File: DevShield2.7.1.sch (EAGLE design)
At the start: 58 parts, among them Q1 BC846BWT1G, SW1 BC-RESET, SW2 ARD-RESET, SW3 RECLAIM, U1 LD1117S33TR, U2 74LVC241A, U3 ETRX357, U4 SN74LVC1G32, U5 ER-OLED9.1, U6 AT45DB041D, X1 ISA HEADER, X3 RASPBERRYPI-V2-HEADERS, X4 1X5

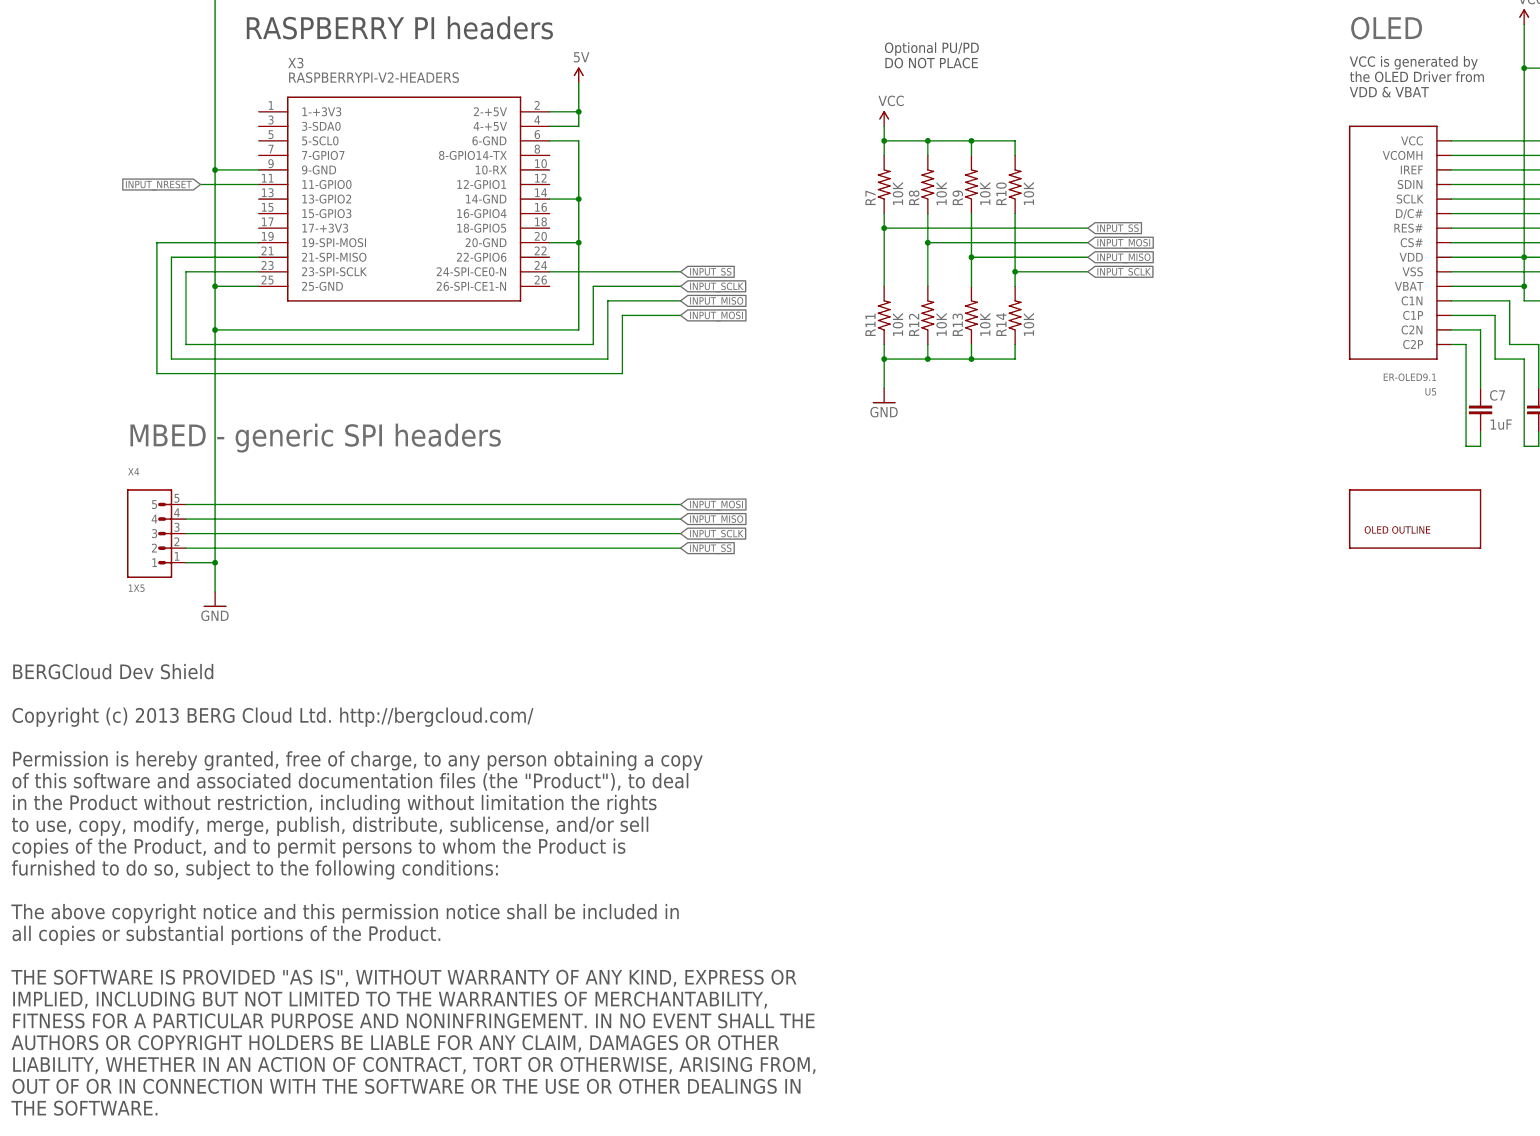
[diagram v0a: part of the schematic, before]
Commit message: Updated Library and pin names for Raspberry Pi
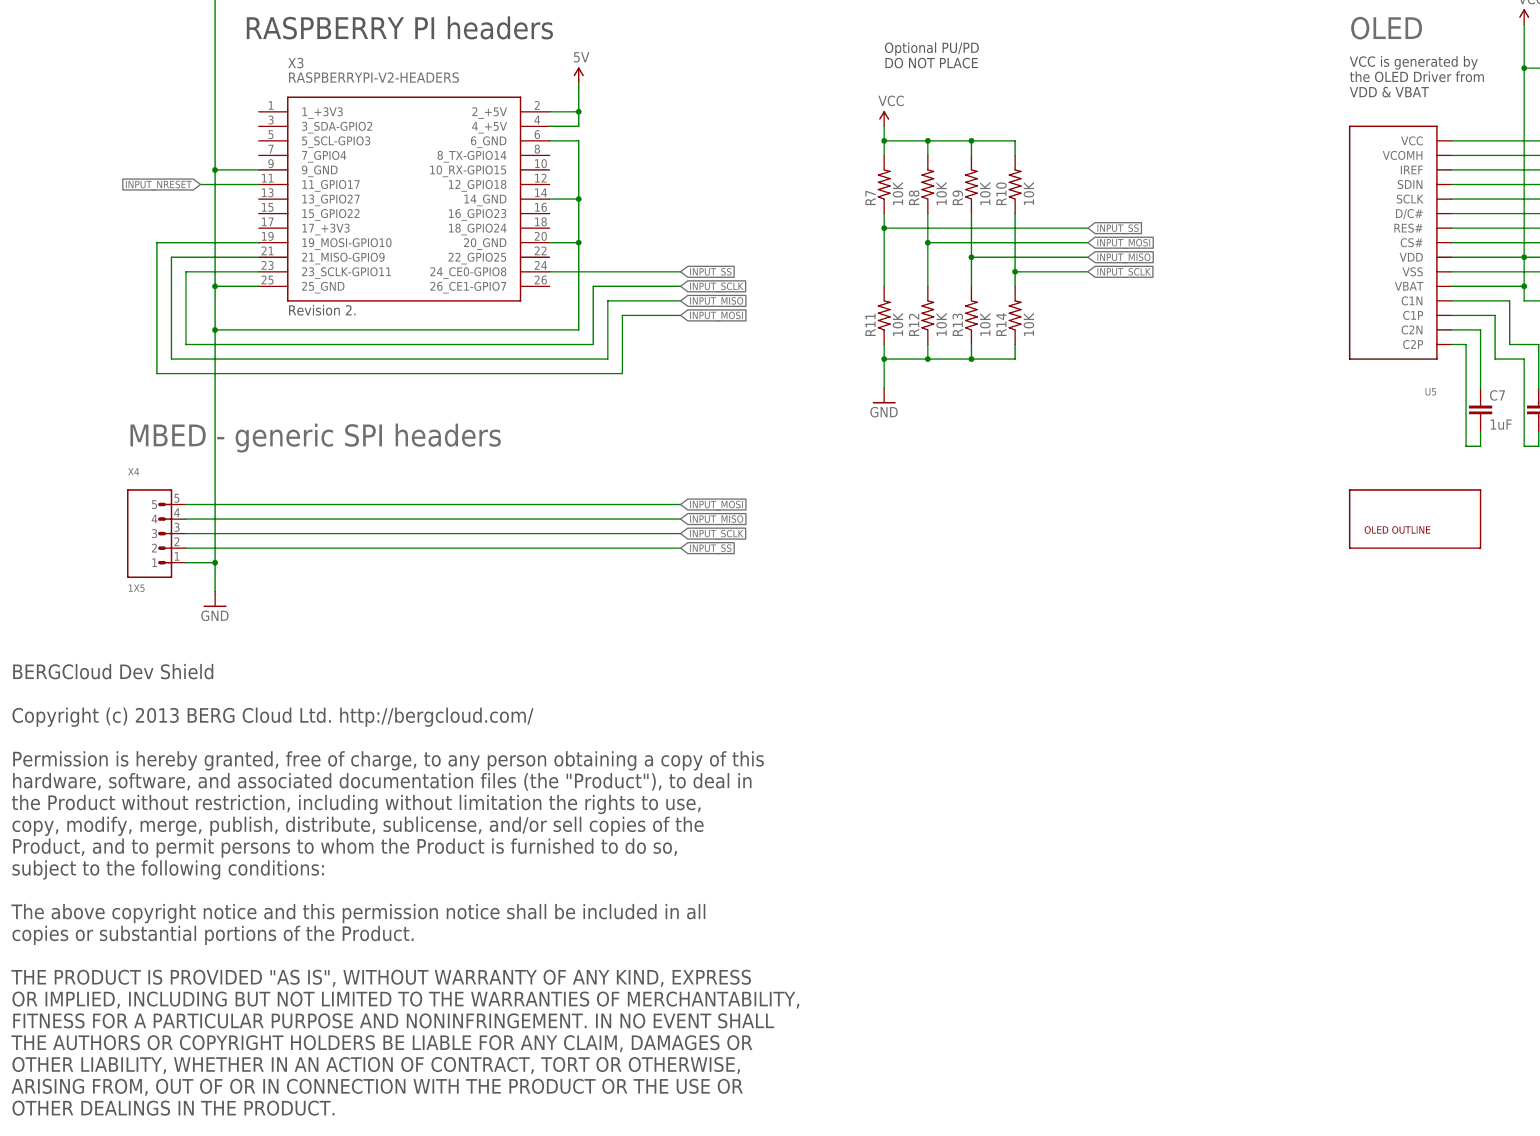
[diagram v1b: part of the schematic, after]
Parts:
- IGNORE: value OLED -> ER-OLED0.91-1-OUTLINE; device BERG-Eagle_Library:OLED -> BERGCloud-OSH:ER-OLED0.91-1-OUTLINE
- Q1: device BERG-Eagle_Library:BC846BWT1GTRANSISTOR -> BERGCloud-OSH:BC846BWT1G
- SW1, SW2: device BERG-Eagle_Library:SPST -> BERGCloud-OSH:SPST
- U1: device BERG-OSH:LD1117S33TR -> BERGCloud-OSH:LD1117S33TR
- U2: device BERG-OSH:74LVC241APW -> BERGCloud-OSH:74LVC241APW
- U3: device BERG-OSH:ETRX35XMODULE-SMD -> BERGCloud-OSH:ETRX35XMODULE-SMD
- U4: device BERG-OSH:74LVC1G32 -> BERGCloud-OSH:74LVC1G32
- U5: value ER-OLED9.1 -> ER-OLED0.91-1HANDSOLDER_BOTTOMLAYER; device BERG-Eagle_Library:ER-OLED9.1 -> BERGCloud-OSH:ER-OLED0.91-1HANDSOLDER_BOTTOMLAYER
- X1: device BERG-OSH:EMBER_ISASHROUDED-1.27MM -> BERGCloud-OSH:EMBER_ISASHROUDED-1.27MM
- X2: device BERG-OSH:ARDUINO_UNO_IO_INCL_ICSP -> BERGCloud-OSH:ARDUINO_UNO_IO_INCL_ICSP
- X3: device BERG-Eagle_Library:RASPBERRY-PI-V2-HEADERSHEADERS -> BERGCloud-OSH:RASPBERRY-PIHEADERS
- X4: device BERG-OSH:1X5 -> BERGCloud-OSH:1X5
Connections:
- net 5V: now also X3.2_+5V, X3.4_+5V; no longer X3.2-+5V, X3.4-+5V
- net GND: now also X3.14_GND, X3.20_GND, X3.25_GND, X3.6_GND, X3.9_GND; no longer X3.14-GND, X3.20-GND, X3.25-GND, X3.6-GND, X3.9-GND
- net INPUT_MISO: now also X3.21_MISO-GPIO9; no longer X3.21-SPI-MISO
- net INPUT_MOSI: now also X3.19_MOSI-GPIO10; no longer X3.19-SPI-MOSI
- net INPUT_NRESET: now also X3.11_GPIO17; no longer X3.11-GPIO0
- net INPUT_SCLK: now also X3.23_SCLK-GPIO11; no longer X3.23-SPI-SCLK
- net INPUT_SS: now also X3.24_CE0-GPIO8; no longer X3.24-SPI-CE0-N
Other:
- note added: "BERGCloud Dev Shield Copyright (c) 2013 BERG Cloud Ltd. http://bergcloud.com/ Permission is hereby granted, free of charge, to any person obtaining a copy of this hardware, software, and associated documentation files (the "Product"), to deal in the Product without restriction, including without limitation the rights to use, copy, modify, merge, publish, distribute, sublicense, and/or sell copies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"
- note removed: "BERGCloud Dev Shield Copyright (c) 2013 BERG Cloud Ltd. http://bergcloud.com/ Permission is hereby granted, free of charge, to any person obtaining a copy of this software and associated documentation files (the "Product"), to deal in the Product without restriction, including without limitation the rights to use, copy, modify, merge, publish, distribute, sublicense, and/or sell copies of the Pro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"
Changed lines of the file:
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@@
 <part name="P+3" library="SparkFun" deviceset="VCC" device=""/>
 <part name="GND6" library="SparkFun" deviceset="GND" device=""/>
-<part name="SW2" library="BERG-Eagle_Library" deviceset="SPST" device="" value="ARD-RESET">
+<part name="SW2" library="BERGCloud-OSH" deviceset="SPST" device="" value="ARD-RESET">
 <attribute name="MF" value="TE CONNECTIVITY / ALCOSWITCH"/>
 <attribute name="MPN" value="FSMSM"/>
@@
 <attribute name="OC_FARNELL" value="unknown"/>
 </part>
-<part name="X3" library="BERG-Eagle_Library" deviceset="RASPBERRY-PI-V2-HEADERS" device="HEADERS" value="RASPBERRYPI-V2-HEADERS">
+<part name="X3" library="BERGCloud-OSH" deviceset="RASPBERRY-PI" device="HEADERS" value="RASPBERRYPI-V2-HEADERS">
 <attribute name="MF" value=""/>
 <attribute name="MPN" value=""/>
@@
 <part name="GND21" library="SparkFun" deviceset="GND" device=""/>
 <part name="P+5" library="SparkFun" deviceset="VCC" device=""/>
-<part name="SW1" library="BERG-Eagle_Library" deviceset="SPST" device="" value="BC-RESET">
+<part name="SW1" library="BERGCloud-OSH" deviceset="SPST" device="" value="BC-RESET">
 <attribute name="MF" value="TE CONNECTIVITY / ALCOSWITCH"/>
 <attribute name="MPN" value="FSMSM"/>
@@
 <attribute name="OC_FARNELL" value="2145384"/>
 </part>
-<part name="IGNORE" library="BERG-Eagle_Library" deviceset="OLED" device="">
-<attribute name="MF" value=""/>
-<attribute name="MPN" value=""/>
-<attribute name="OC_FARNELL" value="unknown"/>
-</part>
-<part name="U5" library="BERG-Eagle_Library" deviceset="ER-OLED9.1" device="">
+<part name="IGNORE" library="BERGCloud-OSH" deviceset="ER-OLED0.91-1-OUTLINE" device="">
+<attribute name="MF" value=""/>
+<attribute name="MPN" value=""/>
+<attribute name="OC_FARNELL" value="unknown"/>
+</part>
+<part name="U5" library="BERGCloud-OSH" deviceset="ER-OLED0.91-1" device="" technology="HANDSOLDER_BOTTOMLAYER" value="">
 <attribute name="MF" value=""/>
 <attribute name="MPN" value=""/>
@@
 <part name="U$5" library="SparkFun" deviceset="5V" device=""/>
 <part name="U$6" library="SparkFun" deviceset="5V" device=""/>
-<part name="Q1" library="BERG-Eagle_Library" deviceset="BC846BWT1GTRANSISTOR" device="" value="BC846BWT1G">
+<part name="Q1" library="BERGCloud-OSH" deviceset="BC846" device="" technology="BWT1G" value="BC846BWT1G">
 <attribute name="MF" value="ON SEMICONDUCTOR"/>
 <attribute name="MPN" value="BC846BWT1G"/>
@@
 <part name="P+8" library="SparkFun" deviceset="VCC" device=""/>
 <part name="GND5" library="SparkFun" deviceset="GND" device=""/>
-<part name="X1" library="BERG-OSH" deviceset="EMBER_ISA" device="SHROUDED-1.27MM" value="ISA HEADER">
-<attribute name="MF" value=""/>
-<attribute name="MPN" value=""/>
-<attribute name="OC_FARNELL" value="unknown"/>
-</part>
-<part name="U3" library="BERG-OSH" deviceset="ETRX35X" device="MODULE-SMD" value="ETRX357">
+<part name="X1" library="BERGCloud-OSH" deviceset="EMBER_ISA" device="SHROUDED-1.27MM" value="ISA HEADER">
+<attribute name="MF" value=""/>
+<attribute name="MPN" value=""/>
+<attribute name="OC_FARNELL" value="unknown"/>
+</part>
+<part name="U3" library="BERGCloud-OSH" deviceset="ETRX35X" device="MODULE-SMD" value="ETRX357">
 <attribute name="MF" value=""/>
 <attribute name="MPN" value=""/>
@@
 </part>
 <part name="FRAME1" library="BERG-OSH" deviceset="A3-FRAME" device=""/>
-<part name="X2" library="BERG-OSH" deviceset="ARDUINO_UNO_IO_INCL_ICSP" device="">
-<attribute name="MF" value=""/>
-<attribute name="MPN" value=""/>
-<attribute name="OC_FARNELL" value="unknown"/>
-</part>
-<part name="U4" library="BERG-OSH" deviceset="74*1G32" device="" technology="LVC" value="SN74LVC1G32">
+<part name="X2" library="BERGCloud-OSH" deviceset="ARDUINO_UNO_IO_INCL_ICSP" device="">
+<attribute name="MF" value=""/>
+<attribute name="MPN" value=""/>
+<attribute name="OC_FARNELL" value="unknown"/>
+</part>
+<part name="U4" library="BERGCloud-OSH" deviceset="74*1G32" device="" technology="LVC" value="SN74LVC1G32">
 <attribute name="MF" value="TEXAS INSTRUMENTS"/>
 <attribute name="MPN" value="SN74LVC1G32DCKR"/>
 <attribute name="OC_FARNELL" value="1470880"/>
 </part>
-<part name="U2" library="BERG-OSH" deviceset="74LVC241A" device="" technology="PW" value="74LVC241A">
+<part name="U2" library="BERGCloud-OSH" deviceset="74LVC241A" device="" technology="PW" value="74LVC241A">
 <attribute name="MF" value=""/>
 <attribute name="MPN" value=""/>
@@
 <attribute name="OC_FARNELL" value="1833840"/>
 </part>
-<part name="X4" library="BERG-OSH" deviceset="1X5" device="">
+<part name="X4" library="BERGCloud-OSH" deviceset="1X5" device="">
 <attribute name="MF" value=""/>
 <attribute name="MPN" value=""/>
@@
 </part>
 <part name="P+1" library="SparkFun" deviceset="VCC" device=""/>
-<part name="U1" library="BERG-OSH" deviceset="LD1117S33TR" device=""/>
+<part name="U1" library="BERGCloud-OSH" deviceset="LD1117S33TR" device=""/>
 </parts>
 <sheets>
@@
 <text x="0" y="-2.54" size="2.54" layer="97" font="vector" align="top-left">BERGCloud Dev Shield
 Copyright (c) 2013 BERG Cloud Ltd. http://bergcloud.com/
-Permission is hereby granted, free of charge, to any person obtaining a copy
-of this software and associated documentation files (the "Product"), to deal
-in the Product without restriction, including without limitation the rights
-to use, copy, modify, merge, publish, distribute, sublicense, and/or sell
-copies of the Product, and to permit persons to whom the Product is
-furnished to do so, subject to the following conditions:
-The above copyright notice and this permission notice shall be included in
-all copies or substantial portions of the Product.
-THE SOFTWARE IS PROVIDED "AS IS", WITHOUT WARRANTY OF ANY KIND, EXPRESS OR
-IMPLIED, INCLUDING BUT NOT LIMITED TO THE WARRANTIES OF MERCHANTABILITY,
-FITNESS FOR A PARTICULAR PURPOSE AND NONINFRINGEMENT. IN NO EVENT SHALL THE
-AUTHORS OR COPYRIGHT HOLDERS BE LIABLE FOR ANY CLAIM, DAMAGES OR OTHER
-LIABILITY, WHETHER IN AN ACTION OF CONTRACT, TORT OR OTHERWISE, ARISING FROM,
-OUT OF OR IN CONNECTION WITH THE SOFTWARE OR THE USE OR OTHER DEALINGS IN
-THE SOFTWARE.</text>
+Permission is hereby granted, free of charge, to any person obtaining a copy of this
+hardware, software, and associated documentation files (the "Product"), to deal in
+the Product without restriction, including without limitation the rights to use,
+copy, modify, merge, publish, distribute, sublicense, and/or sell copies of the
+Product, and to permit persons to whom the Product is furnished to do so,
+subject to the following conditions:
+The above copyright notice and this permission notice shall be included in all
+copies or substantial portions of the Product.
+THE PRODUCT IS PROVIDED "AS IS", WITHOUT WARRANTY OF ANY KIND, EXPRESS
+OR IMPLIED, INCLUDING BUT NOT LIMITED TO THE WARRANTIES OF MERCHANTABILITY,
+FITNESS FOR A PARTICULAR PURPOSE AND NONINFRINGEMENT. IN NO EVENT SHALL
+THE AUTHORS OR COPYRIGHT HOLDERS BE LIABLE FOR ANY CLAIM, DAMAGES OR
+OTHER LIABILITY, WHETHER IN AN ACTION OF CONTRACT, TORT OR OTHERWISE,
+ARISING FROM, OUT OF OR IN CONNECTION WITH THE PRODUCT OR THE USE OR
+OTHER DEALINGS IN THE PRODUCT.</text>
 </plain>
 <instances>
@@
 <pinref part="GND6" gate="1" pin="GND"/>
 <pinref part="SW2" gate="G$1" pin="P$2"/>
-<pinref part="X3" gate="G$1" pin="9-GND"/>
-<pinref part="X3" gate="G$1" pin="25-GND"/>
-<pinref part="X3" gate="G$1" pin="20-GND"/>
-<pinref part="X3" gate="G$1" pin="14-GND"/>
-<pinref part="X3" gate="G$1" pin="6-GND"/>
+<pinref part="X3" gate="G$1" pin="9_GND"/>
+<pinref part="X3" gate="G$1" pin="25_GND"/>
+<pinref part="X3" gate="G$1" pin="20_GND"/>
+<pinref part="X3" gate="G$1" pin="14_GND"/>
+<pinref part="X3" gate="G$1" pin="6_GND"/>
 <pinref part="Q1" gate="G$1" pin="E"/>
 <pinref part="X2" gate="G$1" pin="GND@2"/>
@@
 <wire x1="99.06" y1="91.44" x2="99.06" y2="93.98" width="0.1524" layer="91"/>
 <junction x="99.06" y="93.98"/>
-<pinref part="X3" gate="G$1" pin="2-+5V"/>
-<pinref part="X3" gate="G$1" pin="4-+5V"/>
+<pinref part="X3" gate="G$1" pin="2_+5V"/>
+<pinref part="X3" gate="G$1" pin="4_+5V"/>
 <pinref part="U$5" gate="G$1" pin="5V"/>
 </segment>
@@
 <wire x1="101.6" y1="63.5" x2="116.84" y2="63.5" width="0.1524" layer="91"/>
 <label x="116.84" y="63.5" size="1.27" layer="95" xref="yes"/>
-<pinref part="X3" gate="G$1" pin="23-SPI-SCLK"/>
+<pinref part="X3" gate="G$1" pin="23_SCLK-GPIO11"/>
 </segment>
 <segment>
@@
 <wire x1="93.98" y1="66.04" x2="116.84" y2="66.04" width="0.1524" layer="91"/>
 <label x="116.84" y="66.04" size="1.27" layer="95" xref="yes"/>
-<pinref part="X3" gate="G$1" pin="24-SPI-CE0-N"/>
+<pinref part="X3" gate="G$1" pin="24_CE0-GPIO8"/>
 </segment>
 <segment>
@@
 <wire x1="33.02" y1="81.28" x2="43.18" y2="81.28" width="0.1524" layer="91"/>
 <label x="33.02" y="81.28" size="1.27" layer="95" rot="R180" xref="yes"/>
-<pinref part="X3" gate="G$1" pin="11-GPIO0"/>
+<pinref part="X3" gate="G$1" pin="11_GPIO17"/>
 </segment>
 </net>
@@
 <wire x1="106.68" y1="58.42" x2="116.84" y2="58.42" width="0.1524" layer="91"/>
 <label x="116.84" y="58.42" size="1.27" layer="95" xref="yes"/>
-<pinref part="X3" gate="G$1" pin="19-SPI-MOSI"/>
+<pinref part="X3" gate="G$1" pin="19_MOSI-GPIO10"/>
 </segment>
 <segment>
@@
 <wire x1="104.14" y1="60.96" x2="116.84" y2="60.96" width="0.1524" layer="91"/>
 <label x="116.84" y="60.96" size="1.27" layer="95" xref="yes"/>
-<pinref part="X3" gate="G$1" pin="21-SPI-MISO"/>
-</segment>
-<segment>
+<pinref part="X3" gate="G$1" pin="21_MISO-GPIO9"/>
+</segment>
+<segment>
